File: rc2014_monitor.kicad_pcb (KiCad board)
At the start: 2 copper layers, 99.1 x 49.9 mm, 53 parts, among them J1 Z80 Bus, J2 Pro Bus, J3 USB_B_Micro, J4 M3 Mounting Hole, SW1 Line Selection, SW2 SW_Push, SW3 SW_Push, SW4 Run/Step Mode, U1 74HCT541, U10 LMC555xM, U11 74HCT00, U12 74HCT74, U13 MAX6816, U2 74HCT541, U3 74HCT541, U4 74HCT138, U5 74HCT151, U6 74HCT32, U7 MAX40200AUK, U8 MAX40200AUK, U9 DS1813R-5+T&R

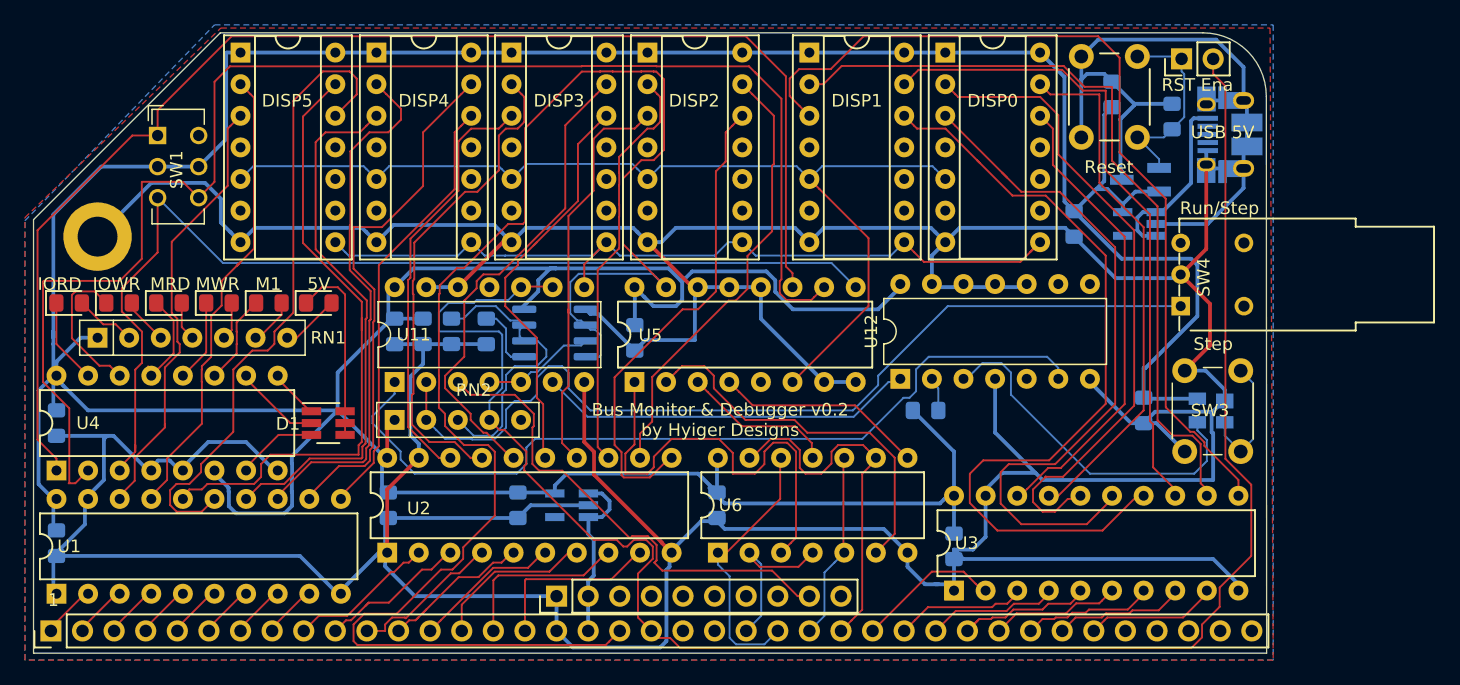
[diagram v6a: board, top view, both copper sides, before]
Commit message: added vias for thermal releaf
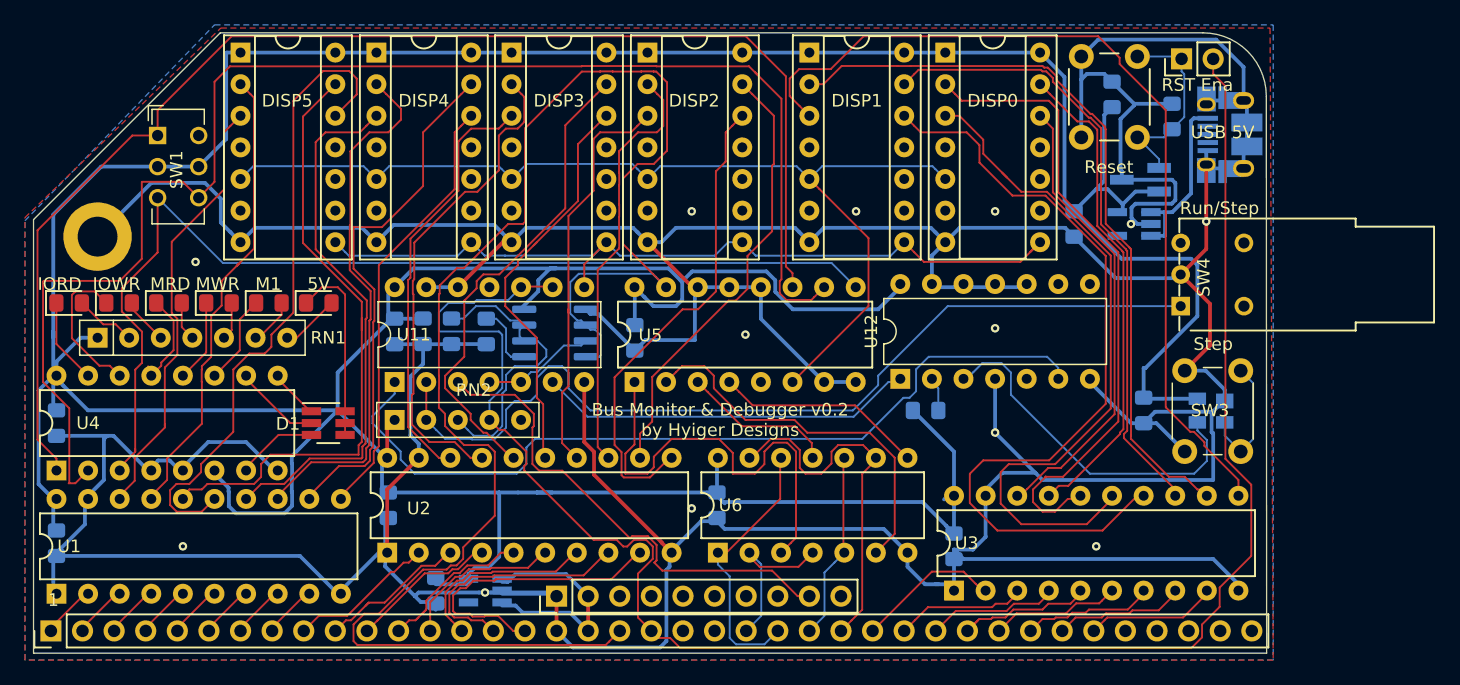
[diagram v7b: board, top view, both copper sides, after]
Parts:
- moved U8 9.76 mm to (112.5, 122.2)
- moved C8 9.53 mm to (108.5, 122.2)
- moved U7 0.43 mm to (164.7, 92.8)
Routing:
- net +5V: track 372.3 -> 384.4 mm
- net A0: track 14.1 -> 24.0 mm
- net GND: track 517.5 -> 509.9 mm, vias 0 -> 13
- net A1: track 14.1 -> 19.7 mm
- net 5V: track 14.1 -> 18.5 mm
- net D_D1: track 42.4 -> 39.3 mm
- net A2: track 12.9 -> 15.4 mm
- net D_D6: track 62.0 -> 60.3 mm
- net Net-(J3-Pad1): track 14.6 -> 16.3 mm
- net D_D5: track 51.7 -> 50.1 mm
- net A3: track 11.7 -> 13.0 mm
- net D_D2: track 52.5 -> 51.7 mm
- net D_A2: track 33.2 -> 34.0 mm
- net D_D0: track 37.8 -> 37.1 mm
- net Net-(SW1-Pad4): track 84.5 -> 83.9 mm
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
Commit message: fixed single step, display hookup
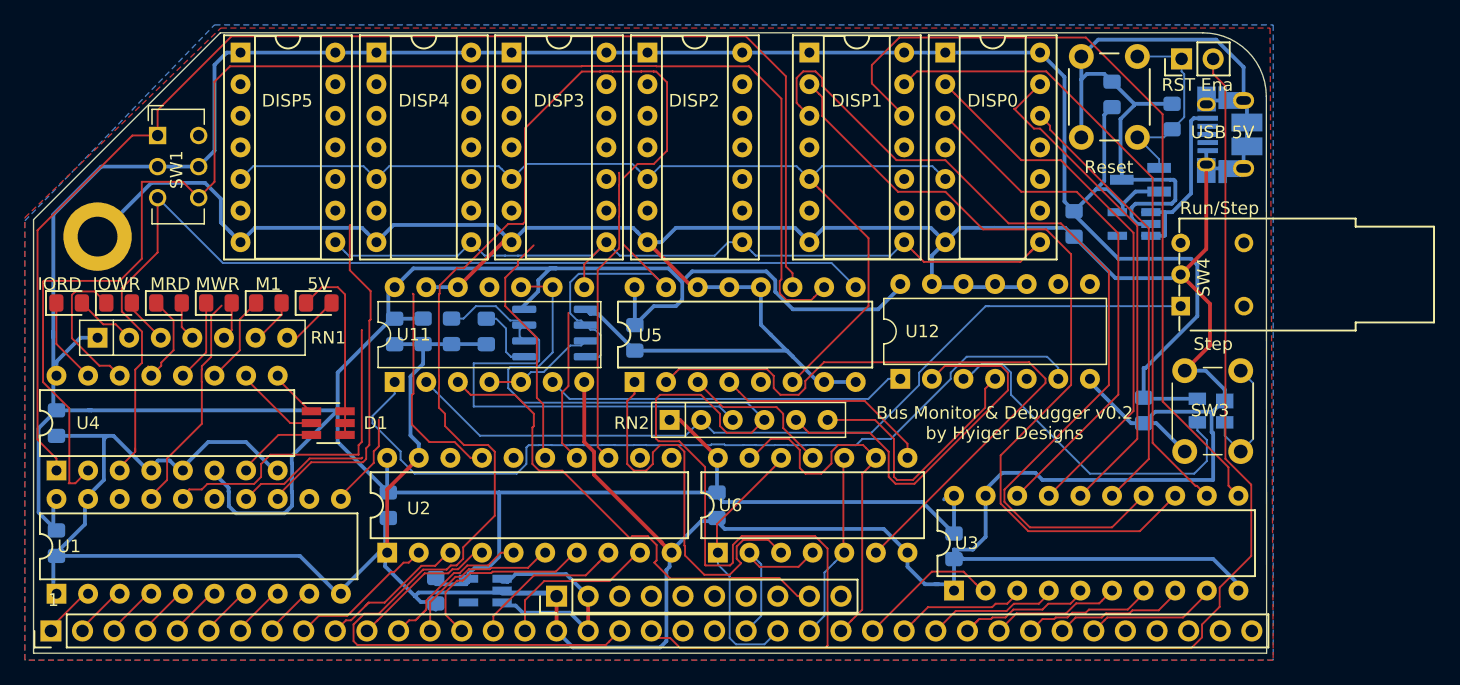
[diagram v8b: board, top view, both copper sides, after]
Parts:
- removed R1: 10K, Resistor_SMD:R_0805_2012Metric_Pad1.15x1.40mm_HandSolder
- RN2: footprint Resistor_THT:R_Array_SIP5 -> Resistor_THT:R_Array_SIP6
- moved RN2 22.1 mm to (127.3, 108.5)
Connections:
- DISP0 pad 12: D_D0 -> D_D3
- DISP0 pad 13: D_D1 -> D_D2
- DISP0 pad 2: D_D2 -> D_D1
- DISP0 pad 3: D_D3 -> D_D0
- DISP1 pad 12: D_D4 -> D_D7
- DISP1 pad 13: D_D5 -> D_D6
- DISP1 pad 2: D_D6 -> D_D5
- DISP1 pad 3: D_D7 -> D_D4
- DISP2 pad 12: D_A0 -> D_A3
- DISP2 pad 13: D_A1 -> D_A2
- DISP2 pad 2: D_A2 -> D_A1
- DISP2 pad 3: D_A3 -> D_A0
- DISP3 pad 12: D_A4 -> D_A7
- DISP3 pad 13: D_A5 -> D_A6
- DISP3 pad 2: D_A6 -> D_A5
- DISP3 pad 3: D_A7 -> D_A4
- DISP4 pad 12: D_A8 -> D_A11
- DISP4 pad 13: D_A9 -> D_A10
- DISP4 pad 2: D_A10 -> D_A9
- DISP4 pad 3: D_A11 -> D_A8
- DISP5 pad 12: D_A12 -> D_A15
- DISP5 pad 13: D_A13 -> D_A14
- DISP5 pad 2: D_A14 -> D_A13
- DISP5 pad 3: D_A15 -> D_A12
- RN2 pad 5: (no net) -> RN2_5
- U12 pad 2: Net-(R1-Pad2) -> RN2_5
- U12 pad 4: GND -> RN2_6
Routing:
- net D_A12: track 52.2 -> 0.00 mm
- net D_A9: track 42.8 -> 0.00 mm
- net D_A0: track 38.7 -> 0.00 mm
- net D_A5: track 38.5 -> 0.00 mm
- net D_A1: track 35.9 -> 0.00 mm
- net D_A15: track 35.4 -> 0.00 mm
- net D_A7: track 34.0 -> 0.00 mm
- net D_A11: track 43.9 -> 10.9 mm
- net RN2_1: track 145.3 -> 177.0 mm
- net RN2_5: track 0.00 -> 31.6 mm
- net D_A8: track 35.5 -> 7.74 mm
- net D_A13: track 50.3 -> 26.6 mm
- net M_RD: track 30.8 -> 53.9 mm
- net D_A6: track 39.4 -> 17.3 mm
- net RN2_6: track 0.00 -> 21.5 mm
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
